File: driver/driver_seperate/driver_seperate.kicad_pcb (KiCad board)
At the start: 4 copper layers, 37.8 x 34.2 mm, 21 parts, among them IC1 MCT8316Z0TQRGFRQ1, J2 Motor, J3 Conn_01x05, J4 Conn_01x02

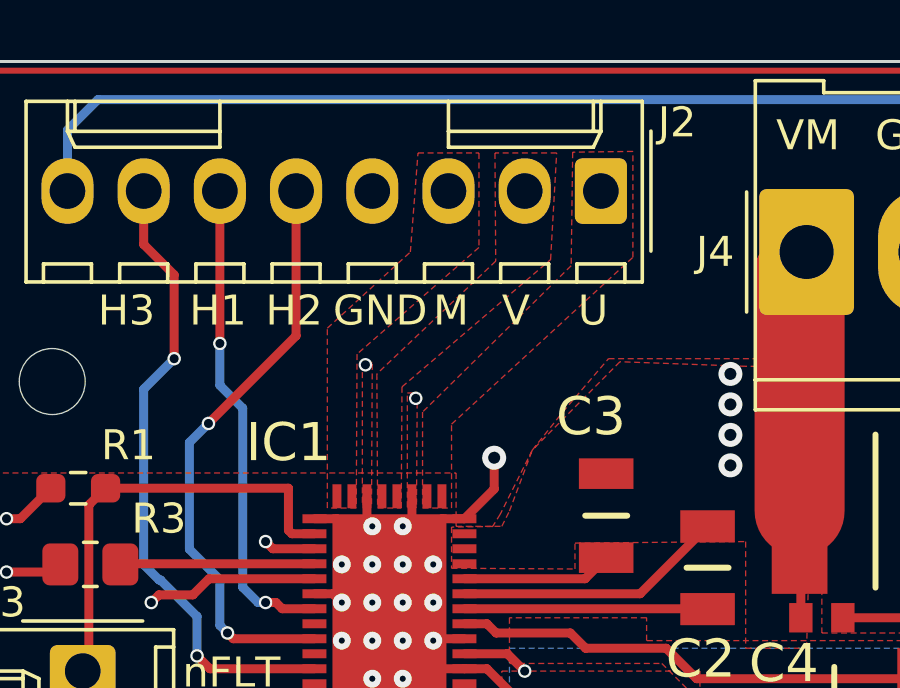
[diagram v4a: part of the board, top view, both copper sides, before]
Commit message: Small U,V,W width change
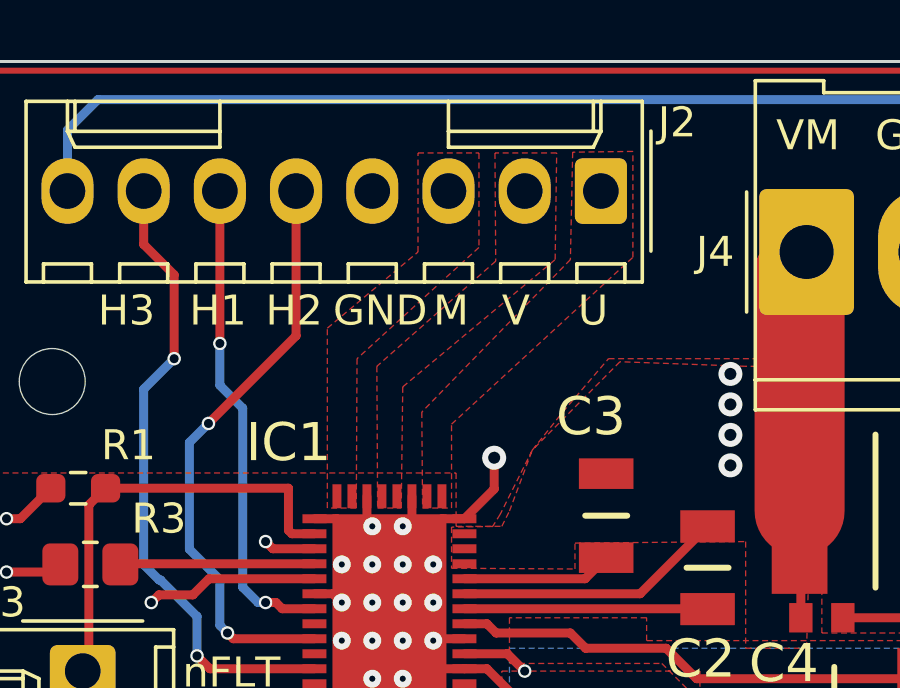
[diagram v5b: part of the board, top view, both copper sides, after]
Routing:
- net GND: vias 25 -> 23
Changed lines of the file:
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@@
   (via (at 121.412 83.312) (size 0.6) (drill 0.2) (layers "F.Cu" "B.Cu") (net 2))
   (via (at 123.444 80.772) (size 0.6) (drill 0.2) (layers "F.Cu" "B.Cu") (net 2))
-  (via (at 123.8758 75.2348) (size 0.45) (drill 0.3) (layers "F.Cu" "B.Cu") (free) (net 2))
   (via (at 122.428 83.312) (size 0.6) (drill 0.2) (layers "F.Cu" "B.Cu") (net 2))
   (via (at 144.78 79.756) (size 0.8) (drill 0.4) (layers "F.Cu" "B.Cu") (free) (net 2))
-  (via (at 122.1994 74.1172) (size 0.45) (drill 0.3) (layers "F.Cu" "B.Cu") (free) (net 2))
   (segment (start 136.164 75.438) (end 136.672 75.946) (width 0.3) (layer "F.Cu") (net 3))
   (segment (start 136.164 76.454) (end 136.672 76.962) (width 0.3) (layer "F.Cu") (net 3))
@@
   (segment (start 119.634 79.634) (end 119.634 78.232) (width 0.3) (layer "F.Cu") (net 27))
   (segment (start 119.634 78.232) (end 113.538 78.232) (width 0.3) (layer "F.Cu") (net 27))
-  (zone (net 2) (net_name "GND") (layer "F.Cu") (hatch edge 0.5)
-    (priority 13)
-    (connect_pads yes (clearance 0.2))
-    (min_thickness 0.25) (filled_areas_thickness no)
-    (fill yes (thermal_gap 0.5) (thermal_bridge_width 0.5))
-    (polygon
-      (pts
-        (xy 123.9012 78.867)
-        (xy 123.5964 78.867)
-        (xy 123.5964 75.057)
-        (xy 123.9266 75.057)
-      )
-    )
-  )
   (zone (net 3) (net_name "/Motor Driver/VM") (layer "F.Cu") (hatch edge 0.5)
     (priority 2)
@@
         (xy 131.1148 67.0052)
         (xy 129.1082 67.0306)
-        (xy 129.0574 70.8152)
-        (xy 124.1044 75.692)
+        (xy 129.032 70.612)
+        (xy 124.079 75.692)
       )
     )
@@
         (xy 122.6058 78.8924)
         (xy 123.3932 78.8924)
-        (xy 123.4186 74.8538)
-        (xy 128.3716 70.612)
+        (xy 123.444 74.8538)
+        (xy 128.524 70.612)
         (xy 128.5748 67.056)
         (xy 126.5174 67.056)
         (xy 126.5428 70.6628)
-        (xy 122.5804 74.422)
+        (xy 122.5804 74.168)
       )
     )
@@
   )
   (zone (net 2) (net_name "GND") (layer "F.Cu") (hatch edge 0.5)
-    (priority 12)
-    (connect_pads yes (clearance 0.2))
-    (min_thickness 0.25) (filled_areas_thickness no)
-    (fill yes (thermal_gap 0.5) (thermal_bridge_width 0.5))
-    (polygon
-      (pts
-        (xy 122.0978 78.7654)
-        (xy 122.4026 78.7654)
-        (xy 122.428 74.041)
-        (xy 122.0978 74.041)
-      )
-    )
-  )
-  (zone (net 2) (net_name "GND") (layer "F.Cu") (hatch edge 0.5)
     (priority 3)
     (connect_pads (clearance 0.5))
@@
         (xy 120.9294 78.8924)
         (xy 120.9294 72.898)
-        (xy 123.698 70.358)
+        (xy 123.952 70.358)
         (xy 123.952 67.056)
         (xy 125.984 67.056)
         (xy 125.984 70.2056)
-        (xy 121.92 73.7616)
-      )
-    )
+        (xy 121.92 73.914)
+      )
+    )

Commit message: Add pcb v2, Remove old files
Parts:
- C1, C4: footprint SamacSys_Parts:CAPC1608X95N -> Capacitor_SMD:C_0805_2012Metric
- C5: value >=10uF -> KCM55TR71H226MH01L
- J3: footprint Connector_Molex:Molex_KK-254_AE-6410-05A_1x05_P2.54mm_Vertical -> Connector_PinSocket_2.54mm:PinSocket_2x03_P2.54mm_Vertical
- moved C4 9.96 mm to (132.3, 74.0), turned to 90 degrees
- moved J3 3.14 mm to (115.1, 86.5), turned to 0 degrees
- moved R6 0.90 mm to (120.0, 90.3)
- moved L1 0.89 mm to (141.5, 87.2)
- moved H1 0.63 mm to (143.9, 95.2)
- moved R7 0.38 mm to (121.5, 90.7)
- moved H2 0.25 mm to (112.0, 74.7)
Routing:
- net /Motor Driver/BRAKE: track 16.1 -> 32.3 mm, vias 2 -> 1
- net GND: track 52.7 -> 45.7 mm
- net /Motor Driver/FGOUT: track 21.4 -> 28.1 mm
- net /Motor Driver/AVDD: track 20.9 -> 15.7 mm
- net /Motor Driver/PWM: track 20.0 -> 15.0 mm
- net /Motor Driver/VM: track 18.8 -> 15.3 mm
- net /Motor Driver/nFault: track 14.8 -> 17.7 mm
- net /Motor Driver/DIR: track 12.8 -> 10.4 mm
- net /Motor Driver/H2: track 19.7 -> 20.5 mm
- net /Motor Driver/H1: track 16.2 -> 16.9 mm
- net /Motor Driver/SW_BK: track 73.7 -> 74.3 mm
- net Net-(IC1-ADVANCE): track 5.45 -> 4.88 mm

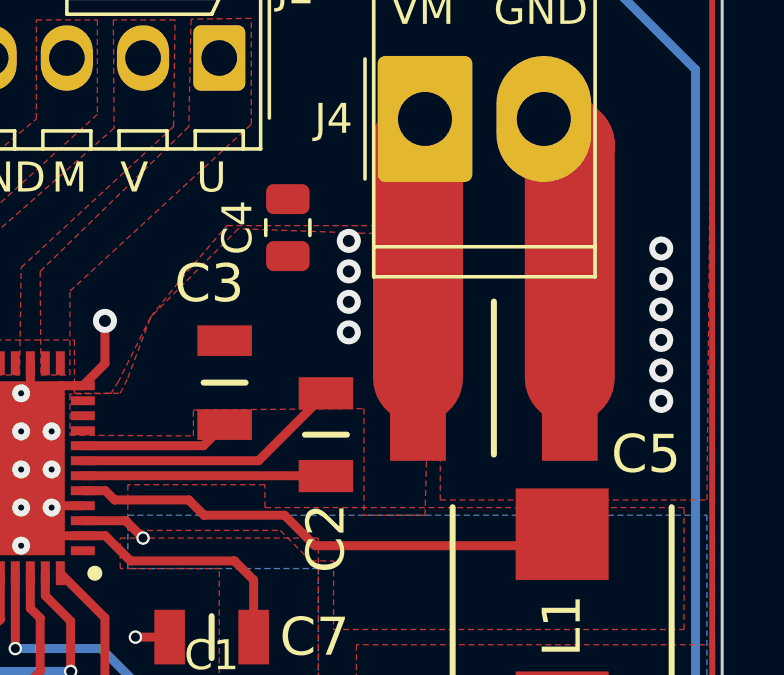
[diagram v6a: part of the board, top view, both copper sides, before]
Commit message: Add motor driver v2
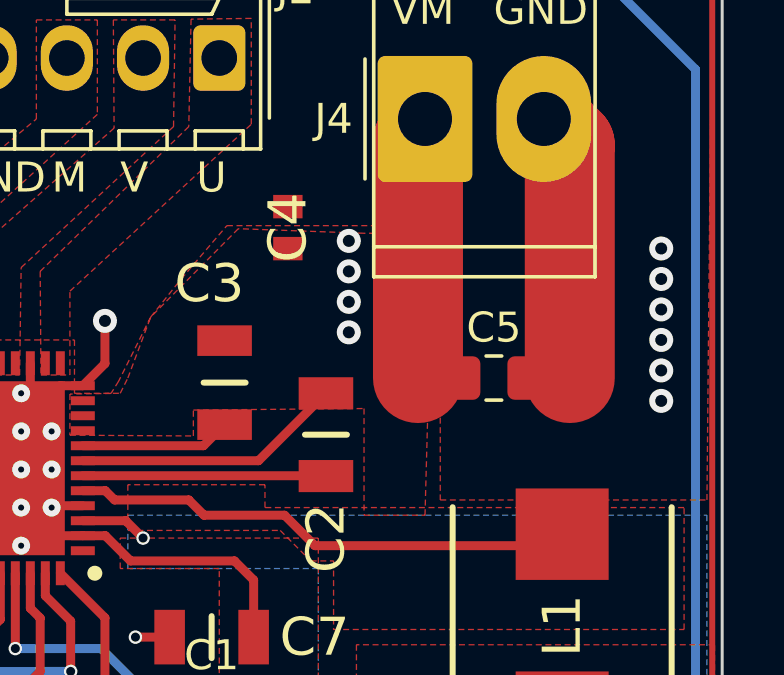
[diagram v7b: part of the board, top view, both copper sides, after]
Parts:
- C4: footprint Capacitor_SMD:C_0805_2012Metric -> SamacSys_Parts:CAPC1608X95N
- C5: footprint SamacSys_Parts:CAPC6153X500N -> Capacitor_SMD:C_0805_2012Metric
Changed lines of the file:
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@@
     )
   )
-  (footprint "Capacitor_SMD:C_0805_2012Metric" (layer "F.Cu")
+  (footprint "SamacSys_Parts:CAPC1608X95N" (layer "F.Cu")
     (at 132.334 73.98 90)
-    (descr "Capacitor SMD 0805 (2012 Metric), square (rectangular) end terminal, IPC_7351 nominal, (Body size source: IPC-SM-782 page 76, https://www.pcb-3d.com/wordpress/wp-content/uploads/ipc-sm-782a_amendment_1_and_2.pdf, https://docs.google.com/spreadsheets/d/1BsfQQcO9C6DZCsRaXUlFlo91Tg2WpOkGARC1WS5S8t0/edit?usp=sharing), generated with kicad-footprint-generator")
-    (tags "capacitor")
+    (descr "0603_2023-1")
+    (tags "Capacitor")
     (property "Sheetfile" "controller.kicad_sch")
     (property "Sheetname" "Motor Driver")
@@
     (property "ki_keywords" "capacitor cap")
     (attr smd)
-    (fp_text reference "C4" (at 0 -1.68 90) (layer "F.SilkS")
-        (effects (font (size 1 1) (thickness 0.15)))
-    )
-    (fp_text value "0u1F" (at 0 1.68 90) (layer "F.Fab")
-        (effects (font (size 1 1) (thickness 0.15)))
+    (fp_text reference "C4" (at 0 0 90) (layer "F.SilkS")
+        (effects (font (size 1.27 1.27) (thickness 0.254)))
+    )
+    (fp_text value "0u1F" (at 0 0 90) (layer "F.SilkS") hide
+        (effects (font (size 1.27 1.27) (thickness 0.254)))
     )
     (fp_text user "${REFERENCE}" (at 0 0 90) (layer "F.Fab")
-        (effects (font (size 0.5 0.5) (thickness 0.08)))
-    )
-    (fp_line (start -0.261252 -0.735) (end 0.261252 -0.735)
-      (stroke (width 0.12) (type solid)) (layer "F.SilkS"))
-    (fp_line (start -0.261252 0.735) (end 0.261252 0.735)
-      (stroke (width 0.12) (type solid)) (layer "F.SilkS"))
-    (fp_line (start -1.7 -0.98) (end 1.7 -0.98)
-      (stroke (width 0.05) (type solid)) (layer "F.CrtYd"))
-    (fp_line (start -1.7 0.98) (end -1.7 -0.98)
-      (stroke (width 0.05) (type solid)) (layer "F.CrtYd"))
-    (fp_line (start 1.7 -0.98) (end 1.7 0.98)
-      (stroke (width 0.05) (type solid)) (layer "F.CrtYd"))
-    (fp_line (start 1.7 0.98) (end -1.7 0.98)
-      (stroke (width 0.05) (type solid)) (layer "F.CrtYd"))
-    (fp_line (start -1 -0.625) (end 1 -0.625)
-      (stroke (width 0.1) (type solid)) (layer "F.Fab"))
-    (fp_line (start -1 0.625) (end -1 -0.625)
-      (stroke (width 0.1) (type solid)) (layer "F.Fab"))
-    (fp_line (start 1 -0.625) (end 1 0.625)
-      (stroke (width 0.1) (type solid)) (layer "F.Fab"))
-    (fp_line (start 1 0.625) (end -1 0.625)
-      (stroke (width 0.1) (type solid)) (layer "F.Fab"))
-    (pad "1" smd roundrect (at -0.95 0 90) (size 1 1.45) (layers "F.Cu" "F.Paste" "F.Mask") (roundrect_rratio 0.25)
+        (effects (font (size 1.27 1.27) (thickness 0.254)))
+    )
+    (fp_line (start -1.24 -0.64) (end 1.24 -0.64)
+      (stroke (width 0.05) (type solid)) (layer "F.CrtYd"))
+    (fp_line (start -1.24 0.64) (end -1.24 -0.64)
+      (stroke (width 0.05) (type solid)) (layer "F.CrtYd"))
+    (fp_line (start 1.24 -0.64) (end 1.24 0.64)
+      (stroke (width 0.05) (type solid)) (layer "F.CrtYd"))
+    (fp_line (start 1.24 0.64) (end -1.24 0.64)
+      (stroke (width 0.05) (type solid)) (layer "F.CrtYd"))
+    (fp_line (start -0.8 -0.4) (end 0.8 -0.4)
+      (stroke (width 0.1) (type solid)) (layer "F.Fab"))
+    (fp_line (start -0.8 0.4) (end -0.8 -0.4)
+      (stroke (width 0.1) (type solid)) (layer "F.Fab"))
+    (fp_line (start 0.8 -0.4) (end 0.8 0.4)
+      (stroke (width 0.1) (type solid)) (layer "F.Fab"))
+    (fp_line (start 0.8 0.4) (end -0.8 0.4)
+      (stroke (width 0.1) (type solid)) (layer "F.Fab"))
+    (pad "1" smd rect (at -0.7 0 90) (size 0.78 0.98) (layers "F.Cu" "F.Paste" "F.Mask")
       (net 3 "/Motor Driver/VM") (pintype "passive"))
-    (pad "2" smd roundrect (at 0.95 0 90) (size 1 1.45) (layers "F.Cu" "F.Paste" "F.Mask") (roundrect_rratio 0.25)
+    (pad "2" smd rect (at 0.7 0 90) (size 0.78 0.98) (layers "F.Cu" "F.Paste" "F.Mask")
       (net 2 "GND") (pintype "passive"))
-    (model "${KICAD6_3DMODEL_DIR}/Capacitor_SMD.3dshapes/C_0805_2012Metric.wrl"
+    (model "C:\\Users\\anton\\projects\\seegoals\\Electronics\\driver\\SamacSys_Parts.3dshapes\\C0603C104K1RACAUTO.stp"
       (offset (xyz 0 0 0))
       (scale (xyz 1 1 1))
@@
     )
   )
-  (footprint "SamacSys_Parts:CAPC6153X500N" (layer "F.Cu")
+  (footprint "Capacitor_SMD:C_0805_2012Metric" (layer "F.Cu")
     (at 139.202 78.994)
-    (descr "KCM55 L=6.1mm W=5.3mm T=4.8mm")
-    (tags "Capacitor")
+    (descr "Capacitor SMD 0805 (2012 Metric), square (rectangular) end terminal, IPC_7351 nominal, (Body size source: IPC-SM-782 page 76, https://www.pcb-3d.com/wordpress/wp-content/uploads/ipc-sm-782a_amendment_1_and_2.pdf, https://docs.google.com/spreadsheets/d/1BsfQQcO9C6DZCsRaXUlFlo91Tg2WpOkGARC1WS5S8t0/edit?usp=sharing), generated with kicad-footprint-generator")
+    (tags "capacitor")
     (property "Sheetfile" "controller.kicad_sch")
     (property "Sheetname" "Motor Driver")
@@
     (property "ki_keywords" "cap capacitor")
     (attr smd)
-    (fp_text reference "C5" (at 5.07 2.54) (layer "F.SilkS")
-        (effects (font (size 1.27 1.27) (thickness 0.254)))
-    )
-    (fp_text value "KCM55TR71H226MH01L" (at 0 0) (layer "F.SilkS") hide
-        (effects (font (size 1.27 1.27) (thickness 0.254)))
+    (fp_text reference "C5" (at 0 -1.68) (layer "F.SilkS")
+        (effects (font (size 1 1) (thickness 0.15)))
+    )
+    (fp_text value "KCM55TR71H226MH01L" (at 0 1.68) (layer "F.Fab")
+        (effects (font (size 1 1) (thickness 0.15)))
     )
     (fp_text user "${REFERENCE}" (at 0 0) (layer "F.Fab")
-        (effects (font (size 1.27 1.27) (thickness 0.254)))
-    )
-    (fp_line (start 0 -2.55) (end 0 2.55)
-      (stroke (width 0.2) (type solid)) (layer "F.SilkS"))
-    (fp_line (start -3.61 -2.91) (end 3.61 -2.91)
-      (stroke (width 0.05) (type solid)) (layer "F.CrtYd"))
-    (fp_line (start -3.61 2.91) (end -3.61 -2.91)
-      (stroke (width 0.05) (type solid)) (layer "F.CrtYd"))
-    (fp_line (start 3.61 -2.91) (end 3.61 2.91)
-      (stroke (width 0.05) (type solid)) (layer "F.CrtYd"))
-    (fp_line (start 3.61 2.91) (end -3.61 2.91)
-      (stroke (width 0.05) (type solid)) (layer "F.CrtYd"))
-    (fp_line (start -3.05 -2.65) (end 3.05 -2.65)
-      (stroke (width 0.1) (type solid)) (layer "F.Fab"))
-    (fp_line (start -3.05 2.65) (end -3.05 -2.65)
-      (stroke (width 0.1) (type solid)) (layer "F.Fab"))
-    (fp_line (start 3.05 -2.65) (end 3.05 2.65)
-      (stroke (width 0.1) (type solid)) (layer "F.Fab"))
-    (fp_line (start 3.05 2.65) (end -3.05 2.65)
-      (stroke (width 0.1) (type solid)) (layer "F.Fab"))
-    (pad "1" smd rect (at -2.53 0) (size 1.86 5.52) (layers "F.Cu" "F.Paste" "F.Mask")
+        (effects (font (size 0.5 0.5) (thickness 0.08)))
+    )
+    (fp_line (start -0.261252 -0.735) (end 0.261252 -0.735)
+      (stroke (width 0.12) (type solid)) (layer "F.SilkS"))
+    (fp_line (start -0.261252 0.735) (end 0.261252 0.735)
+      (stroke (width 0.12) (type solid)) (layer "F.SilkS"))
+    (fp_line (start -1.7 -0.98) (end 1.7 -0.98)
+      (stroke (width 0.05) (type solid)) (layer "F.CrtYd"))
+    (fp_line (start -1.7 0.98) (end -1.7 -0.98)
+      (stroke (width 0.05) (type solid)) (layer "F.CrtYd"))
+    (fp_line (start 1.7 -0.98) (end 1.7 0.98)
+      (stroke (width 0.05) (type solid)) (layer "F.CrtYd"))
+    (fp_line (start 1.7 0.98) (end -1.7 0.98)
+      (stroke (width 0.05) (type solid)) (layer "F.CrtYd"))
+    (fp_line (start -1 -0.625) (end 1 -0.625)
+      (stroke (width 0.1) (type solid)) (layer "F.Fab"))
+    (fp_line (start -1 0.625) (end -1 -0.625)
+      (stroke (width 0.1) (type solid)) (layer "F.Fab"))
+    (fp_line (start 1 -0.625) (end 1 0.625)
+      (stroke (width 0.1) (type solid)) (layer "F.Fab"))
+    (fp_line (start 1 0.625) (end -1 0.625)
+      (stroke (width 0.1) (type solid)) (layer "F.Fab"))
+    (pad "1" smd roundrect (at -0.95 0) (size 1 1.45) (layers "F.Cu" "F.Paste" "F.Mask") (roundrect_rratio 0.25)
       (net 3 "/Motor Driver/VM") (pintype "passive"))
-    (pad "2" smd rect (at 2.53 0) (size 1.86 5.52) (layers "F.Cu" "F.Paste" "F.Mask")
+    (pad "2" smd roundrect (at 0.95 0) (size 1 1.45) (layers "F.Cu" "F.Paste" "F.Mask") (roundrect_rratio 0.25)
       (net 2 "GND") (pintype "passive"))
-    (model "KCM55TR71H226MH01L.stp"
-      (offset (xyz 0 0 0))
-      (scale (xyz 1 1 1))
+    (model "${KICAD6_3DMODEL_DIR}/Capacitor_SMD.3dshapes/C_0805_2012Metric.wrl"
+      (offset (xyz 0 0 0))
+      (scale (xyz 1 1 1))
